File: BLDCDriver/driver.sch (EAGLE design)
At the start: 68 parts, among them CON1 XT30PW-M, Q1 NJM7800S, Q2 SIZ240DT-T1-GE3, Q3 SIZ240DT-T1-GE3, Q4 SIZ240DT-T1-GE3, U1 QFN50P400X400X100-25NDRV8300D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, U2 AS5048A-HTSP-500, U4 SOP80P620X125-8N

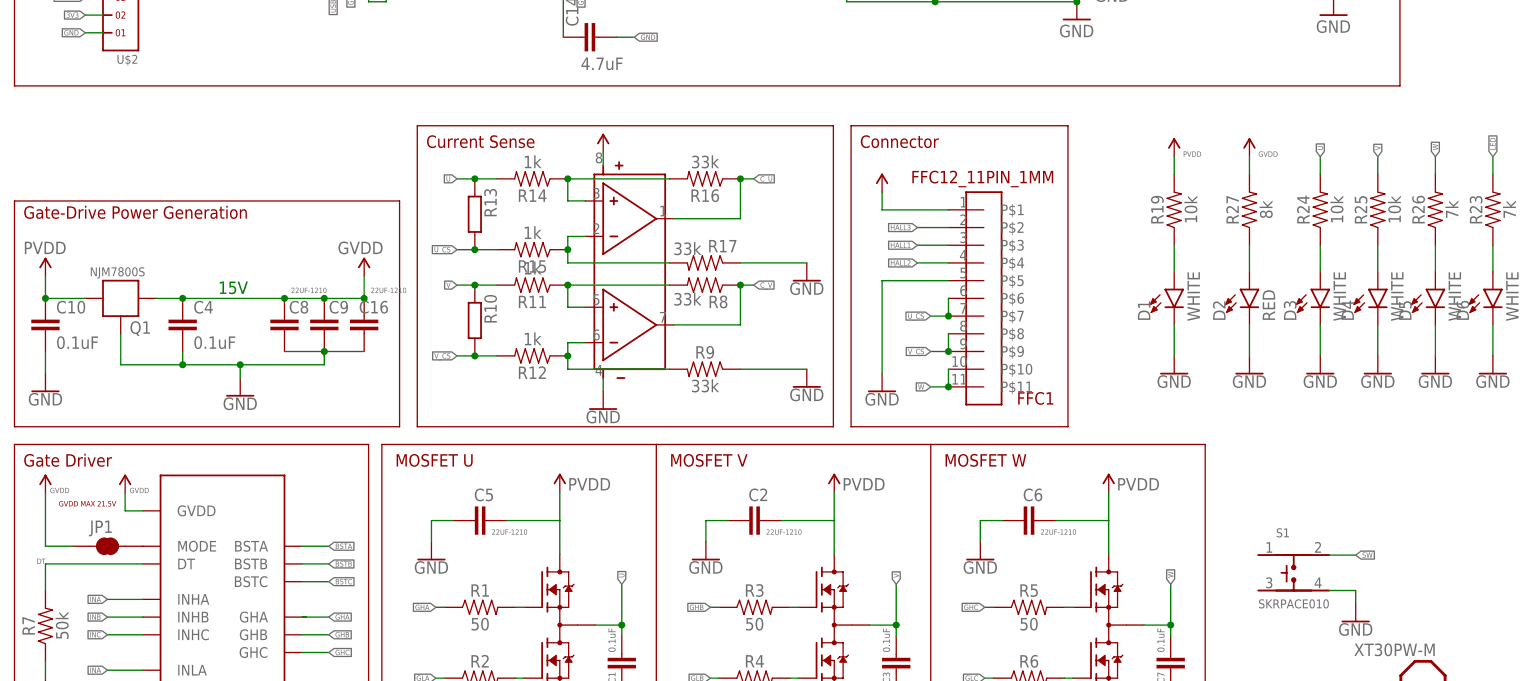
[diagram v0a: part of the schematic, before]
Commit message: モータ固定台のシルク入れた
# ==== Emojis ====
# ✨ :sparkles: Add new feature
# ✅  :white_check_mark: Update existing feature (not bug)
# ⚠️  :warning: Fix bug/error
# 🔥  :fire: Remove files or features
# ✏️ :pencil2: Fix typos
# 📝  :memo: Update documentation
# ♻️  :recycle: Dependencies update
# 🐧  :penguin: Improved the Linux
# 🍎  :apple: Improved the macOS
# 🔖 :bookmark: Add new library
# 🎉  :tada: Initial commit

# ==== Format ====
# :emoji: Subject
#
# Commit body...

# ==== Messages ====
# 新規(ファイル)機能追加: Add
# 機能修正、既存機能追加（バグではない): Update
# リファクタリング: Clean
# ファイル名変更:
# 削除など: Remove
# バグ修正: Fix
# バージョンアップ: Upgrade
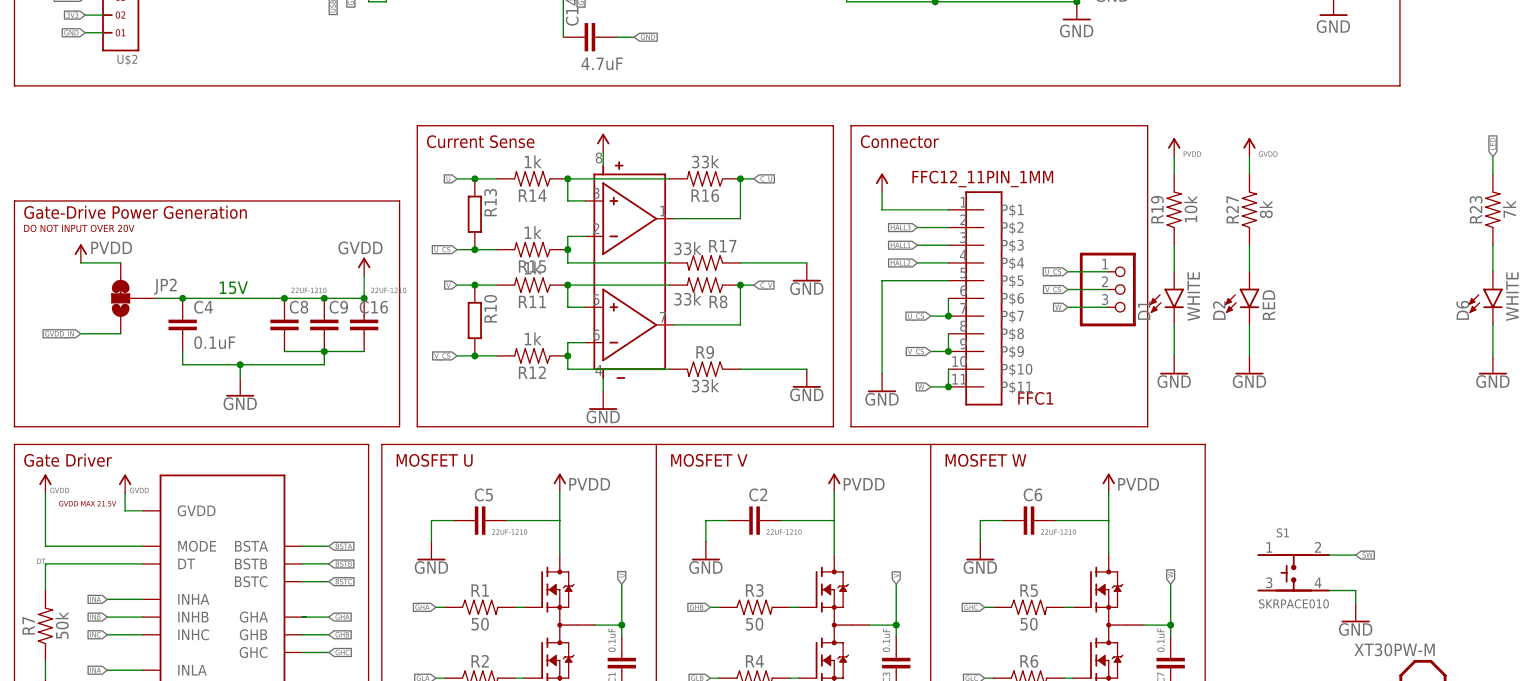
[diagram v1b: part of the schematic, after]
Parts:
- removed C10: 0.1uF, SparkFun-Capacitors:0.1UF-0603-100V-10%
- removed D3, D4, D5: WHITE, SparkFun-LED:LED-WHITE0603
- removed JP1: JUMPER-SMT_2_NC_TRACE_NO-SILK, SparkFun-Jumpers:JUMPER-SMT_2_NC_TRACE_NO-SILK
- removed Q1: NJM7800S, NJM7800S:NJM7800S
- removed R24, R25: 10k, SparkFun-Resistors:2.0KOHM-0603-1/10W-5%
- removed R26: 7k, SparkFun-Resistors:2.0KOHM-0603-1/10W-5%
- added JP2: JUMPER-SMT_3_1-NC_TRACE_SILK, SparkFun-Jumpers:JUMPER-SMT_3_1-NC_TRACE_SILK
- added JP3: (no value), adafruit:PINHD-1X3CB
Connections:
- removed net N$16: D3.A, R24.1
- removed net N$17: D4.A, R25.1
- removed net N$18: D5.A, R26.1
- removed net N$3: JP1.2, U1.MODE
- new net GVDD_IN: JP2.1
- net GND: no longer C10.2, D3.C, D4.C, D5.C, Q1.G
- net GVDD: now also JP2.2, U1.MODE; no longer JP1.1, Q1.O
- net PVDD: now also JP2.3; no longer C10.1, Q1.I
- net U: no longer R24.2
- net U_CS: now also JP3.1
- net V: no longer R25.2
- net V_CS: now also JP3.2
- net W: now also JP3.3; no longer R26.2
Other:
- note added: "DO NOT INPUT OVER 20V"

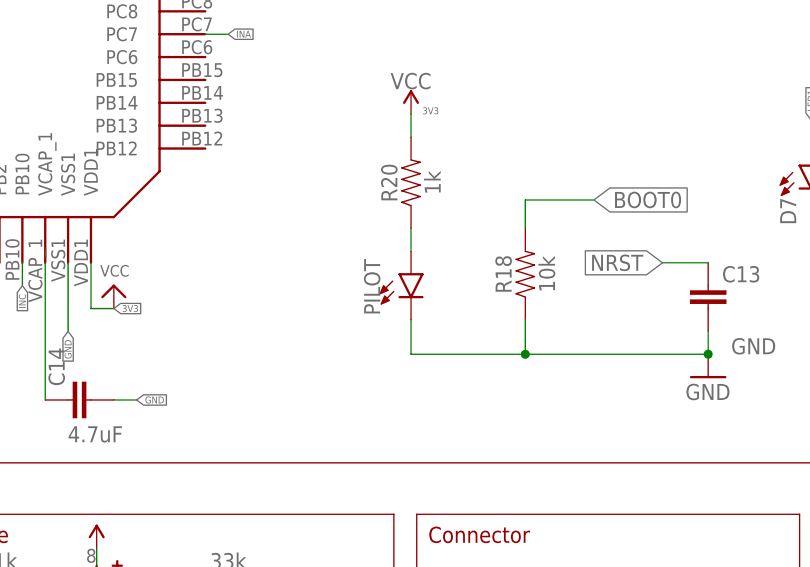
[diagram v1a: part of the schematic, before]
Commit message: シャント抵抗を裏側にした。GVDD消した
# ==== Emojis ====
# ✨ :sparkles: Add new feature
# ✅  :white_check_mark: Update existing feature (not bug)
# ⚠️  :warning: Fix bug/error
# 🔥  :fire: Remove files or features
# ✏️ :pencil2: Fix typos
# 📝  :memo: Update documentation
# ♻️  :recycle: Dependencies update
# 🐧  :penguin: Improved the Linux
# 🍎  :apple: Improved the macOS
# 🔖 :bookmark: Add new library
# 🎉  :tada: Initial commit

# ==== Format ====
# :emoji: Subject
#
# Commit body...

# ==== Messages ====
# 新規(ファイル)機能追加: Add
# 機能修正、既存機能追加（バグではない): Update
# リファクタリング: Clean
# ファイル名変更:
# 削除など: Remove
# バグ修正: Fix
# バージョンアップ: Upgrade
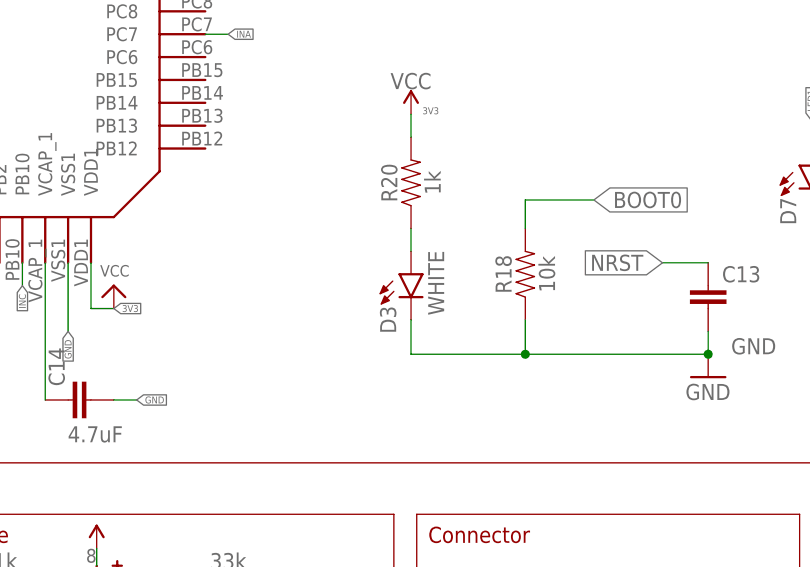
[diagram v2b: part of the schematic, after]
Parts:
- removed PILOT: LED-SMD, Custom_Designed_By_Yusei:LED-SMD
- added D3: WHITE, SparkFun-LED:LED-WHITE0603
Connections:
- net GND: now also D3.C; no longer PILOT.C
- net POWERLED_RESISTOR: now also D3.A; no longer PILOT.A
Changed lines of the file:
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@@
 <part name="R18" library="Custom_Designed_By_Yusei" library_urn="urn:adsk.eagle:library:17377793" deviceset="RESISTOR" device="-0603-1/10W-1%" package3d_urn="urn:adsk.eagle:package:17422883/2" value="10k"/>
 <part name="SUPPLY11" library="SparkFun-PowerSymbols" library_urn="urn:adsk.eagle:library:530" deviceset="VCC" device=""/>
-<part name="PILOT" library="Custom_Designed_By_Yusei" library_urn="urn:adsk.eagle:library:17377793" deviceset="LED-SMD" device="" package3d_urn="urn:adsk.eagle:package:17423055/2" value=""/>
 <part name="R20" library="Custom_Designed_By_Yusei" library_urn="urn:adsk.eagle:library:17377793" deviceset="RESISTOR" device="-0603-1/10W-1%" package3d_urn="urn:adsk.eagle:package:17422883/2" value="1k"/>
 <part name="R21" library="Custom_Designed_By_Yusei" library_urn="urn:adsk.eagle:library:17377793" deviceset="RESISTOR" device="-0603-1/10W-1%" package3d_urn="urn:adsk.eagle:package:17422883/2" value="1k"/>
@@
 <part name="SUPPLY6" library="SparkFun-PowerSymbols" deviceset="VCC_1" device="" value="GVDD"/>
 <part name="JP3" library="adafruit" deviceset="PINHD-1X3" device="CB"/>
+<part name="D3" library="SparkFun-LED" library_urn="urn:adsk.eagle:library:529" deviceset="LED-WHITE" device="0603" package3d_urn="urn:adsk.eagle:package:39354/1" value="WHITE"/>
 </parts>
 <sheets>
@@
 <attribute name="VALUE" x="119.38" y="158.369" size="1.778" layer="96" align="bottom-center"/>
 </instance>
-<instance part="PILOT" gate="G$1" x="119.38" y="137.795" smashed="yes">
-<attribute name="NAME" x="115.951" y="133.223" size="1.778" layer="95" font="vector" rot="R90"/>
-<attribute name="VALUE" x="121.285" y="133.223" size="1.778" layer="96" font="vector" rot="R90" align="top-left"/>
-</instance>
 <instance part="R20" gate="G$1" x="119.38" y="147.955" smashed="yes" rot="R90">
 <attribute name="NAME" x="117.856" y="147.955" size="1.778" layer="95" font="vector" rot="R90" align="bottom-center"/>
@@
 <instance part="JP3" gate="A" x="159.385" y="87.63" smashed="yes">
 <attribute name="VALUE" x="153.035" y="80.01" size="1.778" layer="96"/>
+</instance>
+<instance part="D3" gate="G$1" x="119.38" y="137.795" smashed="yes">
+<attribute name="NAME" x="117.729" y="131.191" size="1.778" layer="95" font="vector" rot="R90"/>
+<attribute name="VALUE" x="121.285" y="133.223" size="1.778" layer="96" font="vector" rot="R90" align="top-left"/>
 </instance>
 </instances>
@@
 <wire x1="132.08" y1="128.905" x2="152.4" y2="128.905" width="0.1524" layer="91"/>
 <junction x="152.4" y="128.905"/>
-<pinref part="PILOT" gate="G$1" pin="C"/>
 <wire x1="119.38" y1="132.715" x2="119.38" y2="128.905" width="0.1524" layer="91"/>
 <wire x1="119.38" y1="128.905" x2="132.08" y2="128.905" width="0.1524" layer="91"/>
 <junction x="132.08" y="128.905"/>
 <label x="154.94" y="128.905" size="1.778" layer="95"/>
+<pinref part="D3" gate="G$1" pin="C"/>
 </segment>
 <segment>
@@
 <segment>
 <pinref part="R20" gate="G$1" pin="1"/>
-<pinref part="PILOT" gate="G$1" pin="A"/>
 <wire x1="119.38" y1="142.875" x2="119.38" y2="140.335" width="0.1524" layer="91"/>
-</segment>
-</net>
+<pinref part="D3" gate="G$1" pin="A"/>
+</segment>
+</net>

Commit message: CANに対応していき
# ==== Emojis ====
# ✨ :sparkles: Add new feature
# ✅  :white_check_mark: Update existing feature (not bug)
# ⚠️  :warning: Fix bug/error
# 🔥  :fire: Remove files or features
# ✏️ :pencil2: Fix typos
# 📝  :memo: Update documentation
# ♻️  :recycle: Dependencies update
# 🐧  :penguin: Improved the Linux
# 🍎  :apple: Improved the macOS
# 🔖 :bookmark: Add new library
# 🎉  :tada: Initial commit

# ==== Format ====
# :emoji: Subject
#
# Commit body...

# ==== Messages ====
# 新規(ファイル)機能追加: Add
# 機能修正、既存機能追加（バグではない): Update
# リファクタリング: Clean
# ファイル名変更:
# 削除など: Remove
# バグ修正: Fix
# バージョンアップ: Upgrade
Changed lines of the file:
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@@
 <setting verticaltext="up"/>
 </settings>
-<grid distance="0.025" unitdist="inch" unit="inch" style="lines" multiple="1" display="no" altdistance="0.01" altunitdist="inch" altunit="inch"/>
+<grid distance="0.1" unitdist="inch" unit="inch" style="lines" multiple="1" display="no" altdistance="0.01" altunitdist="inch" altunit="inch"/>
 <layers>
 <layer number="1" name="Top" color="4" fill="1" visible="no" active="no"/>
@@
 <instance part="R11" gate="G$1" x="74.295" y="88.265" smashed="yes" rot="R180">
 <attribute name="NAME" x="74.295" y="86.741" size="1.778" layer="95" font="vector" rot="R180" align="bottom-center"/>
-<attribute name="VALUE" x="74.295" y="89.789" size="1.778" layer="96" font="vector" rot="R180" align="top-center"/>
+<attribute name="VALUE" x="69.215" y="89.789" size="1.778" layer="96" font="vector" rot="R180" align="top-center"/>
 </instance>
 <instance part="R12" gate="G$1" x="74.295" y="78.105" smashed="yes" rot="R180">

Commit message: 希望が見えてきた
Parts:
- removed C18: (no value), cap-pan40:C-PR-3,5X8
- removed CON1: XT30PW-M, XTn0 amass:XT30PW-M
- added X2: JST-XH-06-PIN-LONG-PAD, Rembrandt Electronics - JST XH Connectors v1-0:JST-XH-06-PIN-LONG-PAD
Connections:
- new net CANH: X2-5.S
- new net CANL: X2-6.S
- net 5V: now also X2-4.S
- net GND: now also X2-3.S; no longer C18.-, CON1.-
- net GVDD_IN: now also X2-1.S
- net PVDD: now also X2-2.S; no longer C18.+, CON1.+
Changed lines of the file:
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@@
 <layer number="56" name="wert" color="7" fill="1" visible="no" active="no"/>
 <layer number="57" name="tCAD" color="7" fill="1" visible="no" active="no"/>
+<layer number="58" name="bCAD" color="7" fill="1" visible="no" active="no"/>
 <layer number="59" name="tCarbon" color="7" fill="1" visible="no" active="no"/>
 <layer number="60" name="bCarbon" color="7" fill="1" visible="no" active="no"/>
@@
 <layer number="154" name="FabDoc2" color="7" fill="1" visible="no" active="no"/>
 <layer number="155" name="FabDoc3" color="7" fill="1" visible="no" active="no"/>
+<layer number="156" name="gesam-Maß" color="7" fill="1" visible="no" active="no"/>
+<layer number="157" name="FaceMchng" color="7" fill="1" visible="no" active="no"/>
+<layer number="158" name="FaceMMeas" color="7" fill="1" visible="no" active="no"/>
+<layer number="159" name="Geh-Bear2" color="7" fill="1" visible="no" active="no"/>
+<layer number="160" name="Topologie" color="7" fill="1" visible="no" active="no"/>
+<layer number="161" name="tomplace2" color="7" fill="1" visible="no" active="no"/>
 <layer number="166" name="AntennaArea" color="7" fill="1" visible="yes" active="yes"/>
 <layer number="168" name="4mmHeightArea" color="7" fill="1" visible="yes" active="yes"/>
@@
 <layer number="250" name="Descript" color="3" fill="1" visible="no" active="no"/>
 <layer number="251" name="SMDround" color="12" fill="11" visible="no" active="no"/>
+<layer number="252" name="BR-BS" color="7" fill="1" visible="no" active="no"/>
+<layer number="253" name="Extra" color="7" fill="1" visible="no" active="no"/>
 <layer number="254" name="cooling" color="7" fill="1" visible="no" active="no"/>
 <layer number="255" name="routoute" color="7" fill="1" visible="no" active="no"/>
@@
 <part name="R23" library="SparkFun-Resistors" library_urn="urn:adsk.eagle:library:532" deviceset="2.0KOHM" device="-0603-1/10W-5%" package3d_urn="urn:adsk.eagle:package:39650/1" value="7k"/>
 <part name="GND25" library="SparkFun-PowerSymbols" deviceset="GND" device=""/>
-<part name="C18" library="cap-pan40" deviceset="C-PR" device="-3,5X8"/>
 <part name="Q2" library="SIZ240DT-T1-GE3" deviceset="SIZ240DT-T1-GE3" device=""/>
 <part name="C1" library="SparkFun-Capacitors" deviceset="0.1UF" device="-0603-25V-5%" value="0.1uF"/>
@@
 <part name="D7" library="SparkFun-LED" library_urn="urn:adsk.eagle:library:529" deviceset="LED-WHITE" device="0603" package3d_urn="urn:adsk.eagle:package:39354/1" value="WHITE"/>
 <part name="D8" library="SparkFun-LED" library_urn="urn:adsk.eagle:library:529" deviceset="LED-WHITE" device="0603" package3d_urn="urn:adsk.eagle:package:39354/1" value="WHITE"/>
-<part name="CON1" library="XTn0 amass" deviceset="XT30" device="PW-M"/>
 <part name="U$2" library="headers(2mm)" deviceset="1X7" device=""/>
 <part name="JP2" library="SparkFun-Jumpers" deviceset="JUMPER-SMT_3_1-NC_TRACE" device="_SILK"/>
@@
 <part name="JP3" library="adafruit" deviceset="PINHD-1X3" device="CB"/>
 <part name="D3" library="SparkFun-LED" library_urn="urn:adsk.eagle:library:529" deviceset="LED-WHITE" device="0603" package3d_urn="urn:adsk.eagle:package:39354/1" value="WHITE"/>
+<part name="X2" library="Rembrandt Electronics - JST XH Connectors v1-0" deviceset="JST-XH-06-PIN" device="-LONG-PAD"/>
 </parts>
 <sheets>
@@
 <attribute name="VALUE" x="212.09" y="75.311" size="1.778" layer="96" align="top-center"/>
 </instance>
-<instance part="C18" gate="G$1" x="187.325" y="15.875" smashed="yes">
-<attribute name="NAME" x="191.008" y="16.3576" size="1.778" layer="95"/>
-<attribute name="VALUE" x="183.0705" y="11.9126" size="1.778" layer="96"/>
-</instance>
 <instance part="Q2" gate="G$1" x="78.232" y="39.497" smashed="yes"/>
 <instance part="C1" gate="G$1" x="87.122" y="35.306" smashed="yes" rot="R180">
@@
 <attribute name="VALUE" x="173.355" y="145.288" size="1.778" layer="96" font="vector" rot="R90" align="top-left"/>
 </instance>
-<instance part="CON1" gate="G$1" x="200.152" y="27.94" smashed="yes" rot="R180">
-<attribute name="VALUE" x="203.962" y="36.83" size="1.778" layer="96" rot="R180"/>
-<attribute name="NAME" x="203.962" y="20.828" size="1.778" layer="95" rot="R180"/>
-</instance>
 <instance part="U$2" gate="G$1" x="15.24" y="132.08" smashed="yes" rot="R180">
 <attribute name="NAME" x="17.78" y="121.285" size="1.27" layer="95" font="vector" rot="R180"/>
@@
 <attribute name="NAME" x="117.729" y="131.191" size="1.778" layer="95" font="vector" rot="R90"/>
 <attribute name="VALUE" x="121.285" y="133.223" size="1.778" layer="96" font="vector" rot="R90" align="top-left"/>
+</instance>
+<instance part="X2" gate="-1" x="187.96" y="68.58" smashed="yes">
+<attribute name="NAME" x="190.5" y="67.818" size="1.524" layer="95"/>
+</instance>
+<instance part="X2" gate="-2" x="187.96" y="66.04" smashed="yes">
+<attribute name="NAME" x="190.5" y="65.278" size="1.524" layer="95"/>
+</instance>
+<instance part="X2" gate="-3" x="187.96" y="63.5" smashed="yes">
+<attribute name="NAME" x="190.5" y="62.738" size="1.524" layer="95"/>
+</instance>
+<instance part="X2" gate="-4" x="187.96" y="60.96" smashed="yes">
+<attribute name="NAME" x="190.5" y="60.198" size="1.524" layer="95"/>
+</instance>
+<instance part="X2" gate="-5" x="187.96" y="58.42" smashed="yes">
+<attribute name="NAME" x="190.5" y="57.658" size="1.524" layer="95"/>
+</instance>
+<instance part="X2" gate="-6" x="187.96" y="55.88" smashed="yes">
+<attribute name="NAME" x="190.5" y="55.118" size="1.524" layer="95"/>
 </instance>
 </instances>
@@
 </segment>
 <segment>
-<pinref part="C18" gate="G$1" pin="-"/>
-<wire x1="184.785" y1="15.875" x2="182.245" y2="15.875" width="0.1524" layer="91"/>
-<label x="182.245" y="15.875" size="0.762" layer="95" rot="R180" xref="yes"/>
-</segment>
-<segment>
-<wire x1="195.072" y1="30.48" x2="193.04" y2="30.48" width="0.1524" layer="91"/>
-<label x="193.04" y="30.48" size="0.762" layer="95" rot="R180" xref="yes"/>
-<pinref part="CON1" gate="G$1" pin="-"/>
-<wire x1="195.072" y1="30.48" x2="195.58" y2="30.48" width="0.1524" layer="91"/>
-</segment>
-<segment>
 <wire x1="117.602" y1="29.337" x2="117.602" y2="24.892" width="0.1524" layer="91"/>
 <pinref part="GND4" gate="1" pin="GND"/>
@@
 <wire x1="12.7" y1="124.46" x2="10.16" y2="124.46" width="0.1524" layer="91"/>
 <label x="10.16" y="124.46" size="0.762" layer="95" rot="R180" xref="yes"/>
+</segment>
+<segment>
+<wire x1="185.42" y1="63.5" x2="182.88" y2="63.5" width="0.1524" layer="91"/>
+<label x="182.88" y="63.5" size="0.762" layer="95" rot="R180" xref="yes"/>
+<pinref part="X2" gate="-3" pin="S"/>
 </segment>
 </net>
@@
 </segment>
 <segment>
-<wire x1="195.072" y1="25.4" x2="193.04" y2="25.4" width="0.1524" layer="91"/>
-<label x="193.04" y="25.4" size="0.762" layer="95" rot="R180" xref="yes"/>
-<pinref part="CON1" gate="G$1" pin="+"/>
-<wire x1="195.072" y1="25.4" x2="195.58" y2="25.4" width="0.1524" layer="91"/>
-</segment>
-<segment>
-<pinref part="C18" gate="G$1" pin="+"/>
-<wire x1="192.405" y1="15.875" x2="194.945" y2="15.875" width="0.1524" layer="91"/>
-<label x="194.945" y="15.875" size="0.762" layer="95" xref="yes"/>
-</segment>
-<segment>
 <pinref part="SUPPLY4" gate="G$2" pin="VCC_1"/>
 <wire x1="117.602" y1="58.547" x2="117.602" y2="54.483" width="0.1524" layer="91"/>
@@
 <label x="10.795" y="92.71" size="1.778" layer="95"/>
 </segment>
+<segment>
+<wire x1="185.42" y1="66.04" x2="182.88" y2="66.04" width="0.1524" layer="91"/>
+<label x="182.88" y="66.04" size="0.762" layer="95" rot="R180" xref="yes"/>
+<pinref part="X2" gate="-2" pin="S"/>
+</segment>
 </net>
 <net name="V" class="0">
@@
 <wire x1="133.985" y1="99.06" x2="124.46" y2="99.06" width="0.1524" layer="91"/>
 <wire x1="124.46" y1="101.6" x2="124.46" y2="99.06" width="0.1524" layer="91"/>
+</segment>
+<segment>
+<wire x1="185.42" y1="60.96" x2="182.88" y2="60.96" width="0.1524" layer="91"/>
+<label x="182.88" y="60.96" size="0.762" layer="95" rot="R180" xref="yes"/>
+<pinref part="X2" gate="-4" pin="S"/>
 </segment>
 </net>
@@
 <label x="9.525" y="81.28" size="0.762" layer="95" rot="R180" xref="yes"/>
 </segment>
-</net>
+<segment>
+<wire x1="185.42" y1="68.58" x2="182.88" y2="68.58" width="0.1524" layer="91"/>
+<label x="182.88" y="68.58" size="0.762" layer="95" rot="R180" xref="yes"/>
+<pinref part="X2" gate="-1" pin="S"/>
+</segment>
+</net>
+<net name="CANH" class="0">
+<segment>
+<wire x1="185.42" y1="58.42" x2="182.88" y2="58.42" width="0.1524" layer="91"/>
+<label x="182.88" y="58.42" size="0.762" layer="95" rot="R180" xref="yes"/>
+<pinref part="X2" gate="-5" pin="S"/>
+</segment>
+</net>
+<net name="CANL" class="0">
+<segment>
+<wire x1="185.42" y1="55.88" x2="182.88" y2="55.88" width="0.1524" layer="91"/>
+<label x="182.88" y="55.88" size="0.762" layer="95" rot="R180" xref="yes"/>
+<pinref part="X2" gate="-6" pin="S"/>
+</segment>
+</net>
